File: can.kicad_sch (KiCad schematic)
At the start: 4 parts, among them J2 5Pin DuPont 2.54mm

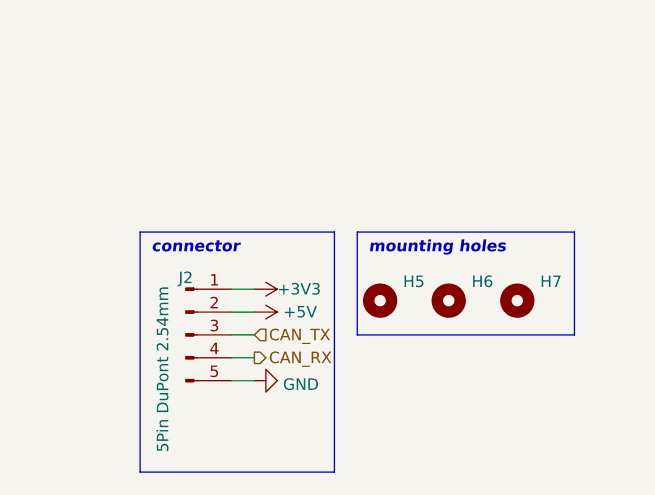
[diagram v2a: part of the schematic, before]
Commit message: Finish PCB layout
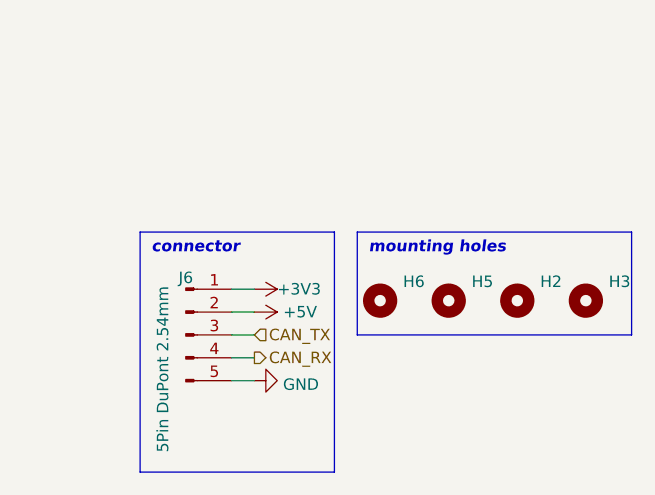
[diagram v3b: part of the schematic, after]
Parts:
- added H3: MountingHole_Pad, extraFootprints:MountingHole_3.2mm_M3_ISO7380_Keepout, symbol Mechanical:MountingHole
- H2: renamed from H7; footprint MountingHole:MountingHole_3.2mm_M3_ISO14580 -> extraFootprints:MountingHole_3.2mm_M3_ISO7380_Keepout
- H5: renamed from H6; footprint MountingHole:MountingHole_3.2mm_M3_ISO14580 -> extraFootprints:MountingHole_3.2mm_M3_ISO7380_Keepout
- H6: renamed from H5; footprint MountingHole:MountingHole_3.2mm_M3_ISO14580 -> extraFootprints:MountingHole_3.2mm_M3_ISO7380_Keepout
- renumbered J2 to J6
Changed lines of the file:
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@@
     (stroke (width 0) (type default) (color 0 0 0 0))
   )
-  (polyline (pts (xy 127 59.69) (xy 151.13 59.69))
+  (polyline (pts (xy 127 59.69) (xy 157.48 59.69))
     (stroke (width 0) (type default) (color 0 0 0 0))
   )
-  (polyline (pts (xy 151.13 71.12) (xy 151.13 59.69))
+  (polyline (pts (xy 157.48 71.12) (xy 157.48 59.69))
     (stroke (width 0) (type default) (color 0 0 0 0))
   )
@@
     (stroke (width 0) (type default) (color 0 0 0 0))
   )
-  (polyline (pts (xy 127 71.12) (xy 151.13 71.12))
+  (polyline (pts (xy 127 71.12) (xy 157.48 71.12))
     (stroke (width 0) (type default) (color 0 0 0 0))
   )
@@
   (symbol (lib_id "Mechanical:MountingHole") (at 137.16 67.31 0) (unit 1)
     (in_bom yes) (on_board yes) (fields_autoplaced)
-    (property "Reference" "H6" (id 0) (at 139.7 65.2053 0)
+    (property "Reference" "H5" (id 0) (at 139.7 65.2053 0)
       (effects (font (size 1.27 1.27)) (justify left))
     )
@@
       (effects (font (size 1.27 1.27)) (justify left) hide)
     )
-    (property "Footprint" "MountingHole:MountingHole_3.2mm_M3_ISO14580" (id 2) (at 137.16 67.31 0)
+    (property "Footprint" "extraFootprints:MountingHole_3.2mm_M3_ISO7380_Keepout" (id 2) (at 137.16 67.31 0)
       (effects (font (size 1.27 1.27)) hide)
     )
@@
   (symbol (lib_id "power:+5V") (at 115.57 68.58 270) (unit 1)
     (in_bom yes) (on_board yes)
-    (property "Reference" "#PWR0118" (id 0) (at 111.76 68.58 0)
+    (property "Reference" "#PWR021" (id 0) (at 111.76 68.58 0)
       (effects (font (size 1.27 1.27)) hide)
     )
@@
   (symbol (lib_id "power:GND") (at 115.57 76.2 90) (unit 1)
     (in_bom yes) (on_board yes) (fields_autoplaced)
-    (property "Reference" "#PWR0120" (id 0) (at 121.92 76.2 0)
+    (property "Reference" "#PWR022" (id 0) (at 121.92 76.2 0)
       (effects (font (size 1.27 1.27)) hide)
     )
@@
     (pin "1")
   )
+  (symbol (lib_id "Mechanical:MountingHole") (at 152.4 67.31 0) (unit 1)
+    (in_bom yes) (on_board yes) (fields_autoplaced)
+    (property "Reference" "H3" (id 0) (at 154.94 65.2053 0)
+      (effects (font (size 1.27 1.27)) (justify left))
+    )
+    (property "Value" "MountingHole_Pad" (id 1) (at 154.94 67.7422 0)
+      (effects (font (size 1.27 1.27)) (justify left) hide)
+    )
+    (property "Footprint" "extraFootprints:MountingHole_3.2mm_M3_ISO7380_Keepout" (id 2) (at 152.4 67.31 0)
+      (effects (font (size 1.27 1.27)) hide)
+    )
+    (property "Datasheet" "~" (id 3) (at 152.4 67.31 0)
+      (effects (font (size 1.27 1.27)) hide)
+    )
+  )
   (symbol (lib_id "Mechanical:MountingHole") (at 144.78 67.31 0) (unit 1)
     (in_bom yes) (on_board yes) (fields_autoplaced)
-    (property "Reference" "H7" (id 0) (at 147.32 65.2053 0)
+    (property "Reference" "H2" (id 0) (at 147.32 65.2053 0)
       (effects (font (size 1.27 1.27)) (justify left))
     )
@@
       (effects (font (size 1.27 1.27)) (justify left) hide)
     )
-    (property "Footprint" "MountingHole:MountingHole_3.2mm_M3_ISO14580" (id 2) (at 144.78 67.31 0)
+    (property "Footprint" "extraFootprints:MountingHole_3.2mm_M3_ISO7380_Keepout" (id 2) (at 144.78 67.31 0)
       (effects (font (size 1.27 1.27)) hide)
     )
@@
   (symbol (lib_id "power:+3V3") (at 115.57 66.04 270) (unit 1)
     (in_bom yes) (on_board yes)
-    (property "Reference" "#PWR0119" (id 0) (at 111.76 66.04 0)
+    (property "Reference" "#PWR020" (id 0) (at 111.76 66.04 0)
       (effects (font (size 1.27 1.27)) hide)
     )
@@
   (symbol (lib_id "Connector:Conn_01x05_Male") (at 107.95 71.12 0) (unit 1)
     (in_bom yes) (on_board yes)
-    (property "Reference" "J2" (id 0) (at 107.95 64.77 0))
+    (property "Reference" "J6" (id 0) (at 107.95 64.77 0))
     (property "Value" "5Pin DuPont 2.54mm" (id 1) (at 105.41 74.93 90))
     (property "Footprint" "Connector_PinHeader_2.54mm:PinHeader_1x05_P2.54mm_Vertical" (id 2) (at 107.95 71.12 0)
@@
   (symbol (lib_id "Mechanical:MountingHole") (at 129.54 67.31 0) (unit 1)
     (in_bom yes) (on_board yes) (fields_autoplaced)
-    (property "Reference" "H5" (id 0) (at 132.08 65.2053 0)
+    (property "Reference" "H6" (id 0) (at 132.08 65.2053 0)
       (effects (font (size 1.27 1.27)) (justify left))
     )
@@
       (effects (font (size 1.27 1.27)) (justify left) hide)
     )
-    (property "Footprint" "MountingHole:MountingHole_3.2mm_M3_ISO14580" (id 2) (at 129.54 67.31 0)
+    (property "Footprint" "extraFootprints:MountingHole_3.2mm_M3_ISO7380_Keepout" (id 2) (at 129.54 67.31 0)
       (effects (font (size 1.27 1.27)) hide)
     )

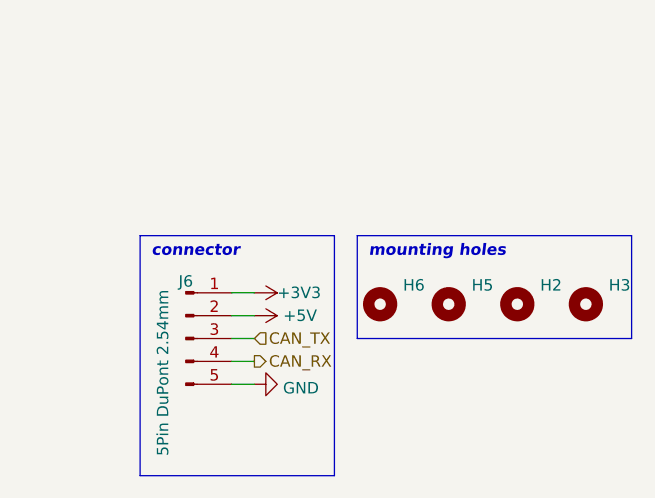
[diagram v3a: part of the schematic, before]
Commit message: Apply suggestions from tux: Single connector for signals Some (better) notes
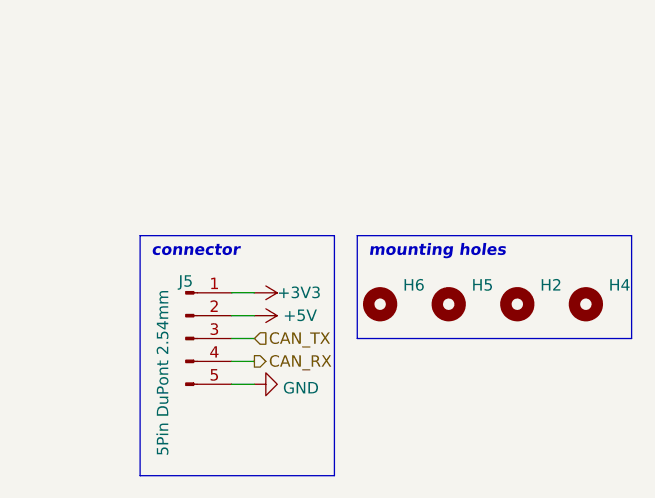
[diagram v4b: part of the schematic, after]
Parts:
- renumbered H3 to H4, J6 to J5
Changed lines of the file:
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@@
   (symbol (lib_id "Mechanical:MountingHole") (at 152.4 67.31 0) (unit 1)
     (in_bom yes) (on_board yes) (fields_autoplaced)
-    (property "Reference" "H3" (id 0) (at 154.94 65.2053 0)
+    (property "Reference" "H4" (id 0) (at 154.94 65.2053 0)
       (effects (font (size 1.27 1.27)) (justify left))
     )
@@
   (symbol (lib_id "Connector:Conn_01x05_Male") (at 107.95 71.12 0) (unit 1)
     (in_bom yes) (on_board yes)
-    (property "Reference" "J6" (id 0) (at 107.95 64.77 0))
+    (property "Reference" "J5" (id 0) (at 107.95 64.77 0))
     (property "Value" "5Pin DuPont 2.54mm" (id 1) (at 105.41 74.93 90))
     (property "Footprint" "Connector_PinHeader_2.54mm:PinHeader_1x05_P2.54mm_Vertical" (id 2) (at 107.95 71.12 0)
